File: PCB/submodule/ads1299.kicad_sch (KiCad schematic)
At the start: 18 parts, among them J20 Conn_01x03, J21 CONN_SUBMODULES, U1 ADS1299IPAG, U2 OPA2376

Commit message: Power supply & TPDs
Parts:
- removed C1: 1uF, symbol Device:C
- removed C2: C, symbol Device:C
- removed J20: Conn_01x03, symbol Connector_Generic:Conn_01x05
- removed unit 3 of U2
- added C14, C16, C17, C18, C19, C20, C21, C22: 4.7uF, symbol Device:C
- added C29: 0.1uF, symbol Device:C
- added C30: 10uF, symbol Device:C
- added C31, C33: 1uF, symbol Device:C
- added C32: 100uF, symbol Device:C
- added J1, J18, J19, J2, J3, J4, J5, J8: Conn_01x01_Pin, symbol Connector:Conn_01x01_Pin
- added JP10, JP11, JP12, JP13, JP14, JP15, JP8, JP9: SolderJumper_2_Bridged, symbol Jumper:SolderJumper_2_Bridged
- added R14, R16, R17: 10k, symbol Device:R
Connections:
- net AGND: now also U1.25 (VREFN), C14.1, C16.1, C17.1, C18.1, C19.1, C20.1, C21.1, C22.1, C29.2, C30.2, C31.2, C32.2, C33.2, JP10.1 (A), JP11.1 (A), JP12.1 (A), JP13.1 (A), JP14.1 (A), JP15.1 (A), JP8.1 (A), JP9.1 (A)
- net DGND: now also U1.31 (RESV1), U1.49 (DGND), U1.51 (DGND), R17.1
- net IN1-: now also C22.2, J19.1 (Pin_1), JP15.2 (B)
- net IN2-: now also C21.2, J18.1 (Pin_1), JP14.2 (B)
- net IN3-: now also C20.2, J8.1 (Pin_1), JP13.2 (B)
- net IN4-: now also C19.2, J5.1 (Pin_1), JP12.2 (B)
- net IN5-: now also C18.2, J4.1 (Pin_1), JP11.2 (B)
- net IN6-: now also C17.2, J3.1 (Pin_1), JP10.2 (B)
- net IN7-: now also C16.2, J2.1 (Pin_1), JP9.2 (B)
- net IN8-: now also C14.2, J1.1 (Pin_1), JP8.2 (B)
- net AVDD: now reaches U1.19 (AVDD)
- net AVDD: now also U1.21 (AVDD), U1.22 (AVDD)
- net AVSS: now reaches U1.20 (AVSS)
- net AVSS: now also U1.23 (AVSS), U1.32 (AVSS)
- net at U1.24 (VREFP): now also C29.1, C30.1
- net at U1.26 (VCAP4): now also C31.1
- net at U1.28 (VCAP1): now also C33.1
- net at U1.30 (VCAP2): now also C32.1
- net PWDN: now reaches U1.35 (*PWDN)
- net PWDN: now also R14.1
- net RESET: now reaches U1.36 (*RESET)
- net RESET: now also R16.1
- net START: now reaches U1.38 (START)
- net START: now also R17.2
- net GPIO1: now reaches U1.42 (GPIO1)
- net GPIO2: now reaches U1.44 (GPIO2)
- net GPIO3: now reaches U1.45 (GPIO3)
- net GPIO4: now reaches U1.46 (GPIO4)
- net DVDD: now reaches U1.48 (DVDD)
- net DVDD: now also U1.50 (DVDD), R14.2, R16.2
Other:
- note added: "CONECTOR AL OTRO SUBMODULO OJOOO! AGREGAR ALIMENTACION"
- note added: "Optional Differential Inputs"
- note added: "SB_DAISY_MODE SB_DATAOUT: - BASE = 2-3 | 2-3 - AUX = 2-1 | 2-1 #Ref. ADS1299 datasheet: Section 10.1.4.2 TODO: Tabla"
- note removed: "AGREGAR CAP Y SB PARA CANALES N"
- note removed: "Agregar DGND al micro"
- note removed: "CONECTOR A MICRO"
- note removed: "CONECTOR AL OTRO SUBMODULO"
- note removed: "Consideramos las alimentaciones resuetlas en la placa main"
- note removed: "OJO! Agregar gitignore para KICAD"
- note removed: "SB_DAISY_MODE SB_DATAOUT: - BASE = 2-3 | 2-3 - AUX = 2-1 | 2-1 #Ref. datasheet: Section 10.1.4.2 TODO: Tabla"
- moved on the sheet: C3

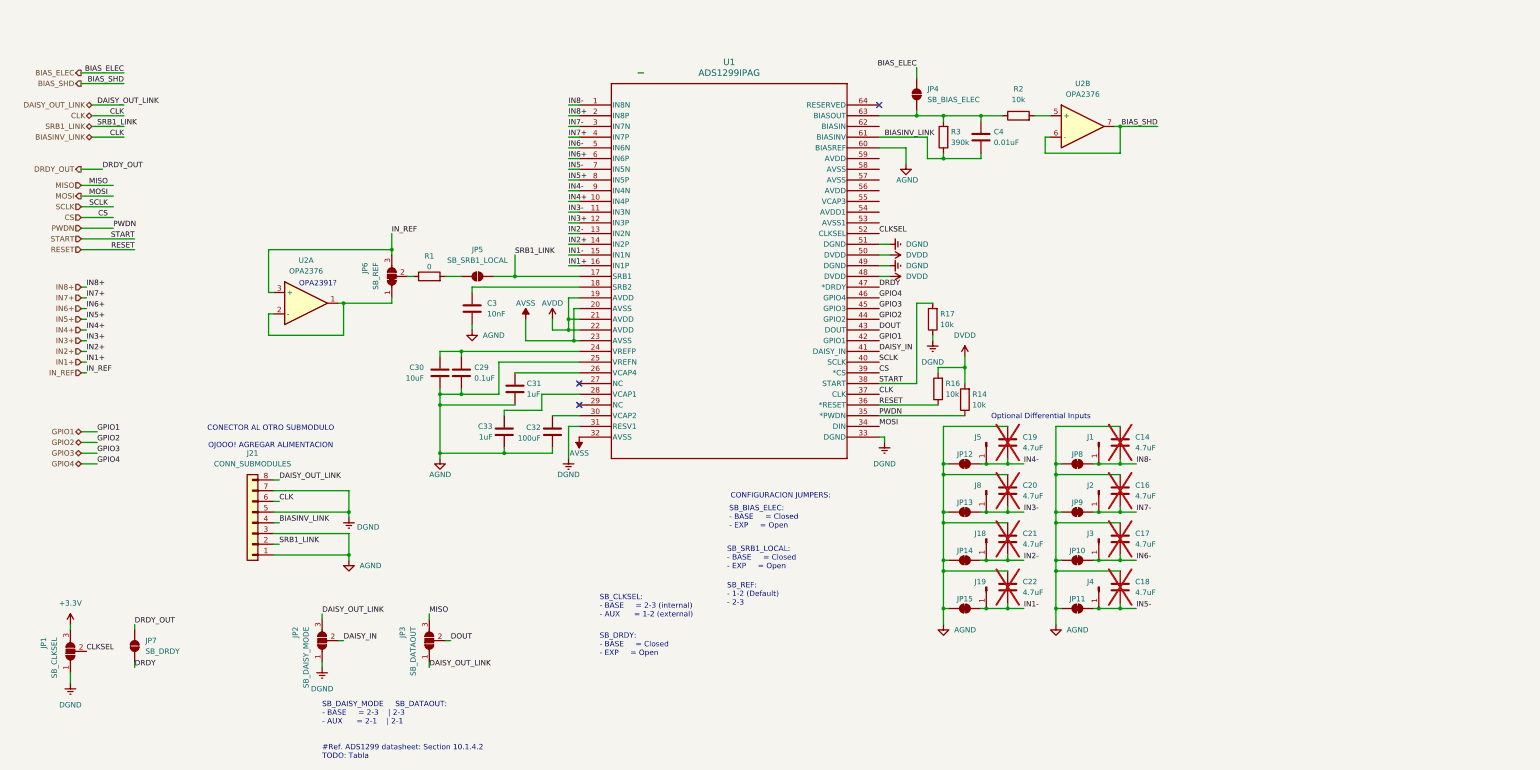
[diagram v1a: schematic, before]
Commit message: draft initial wiring for submodule (pending pin check)
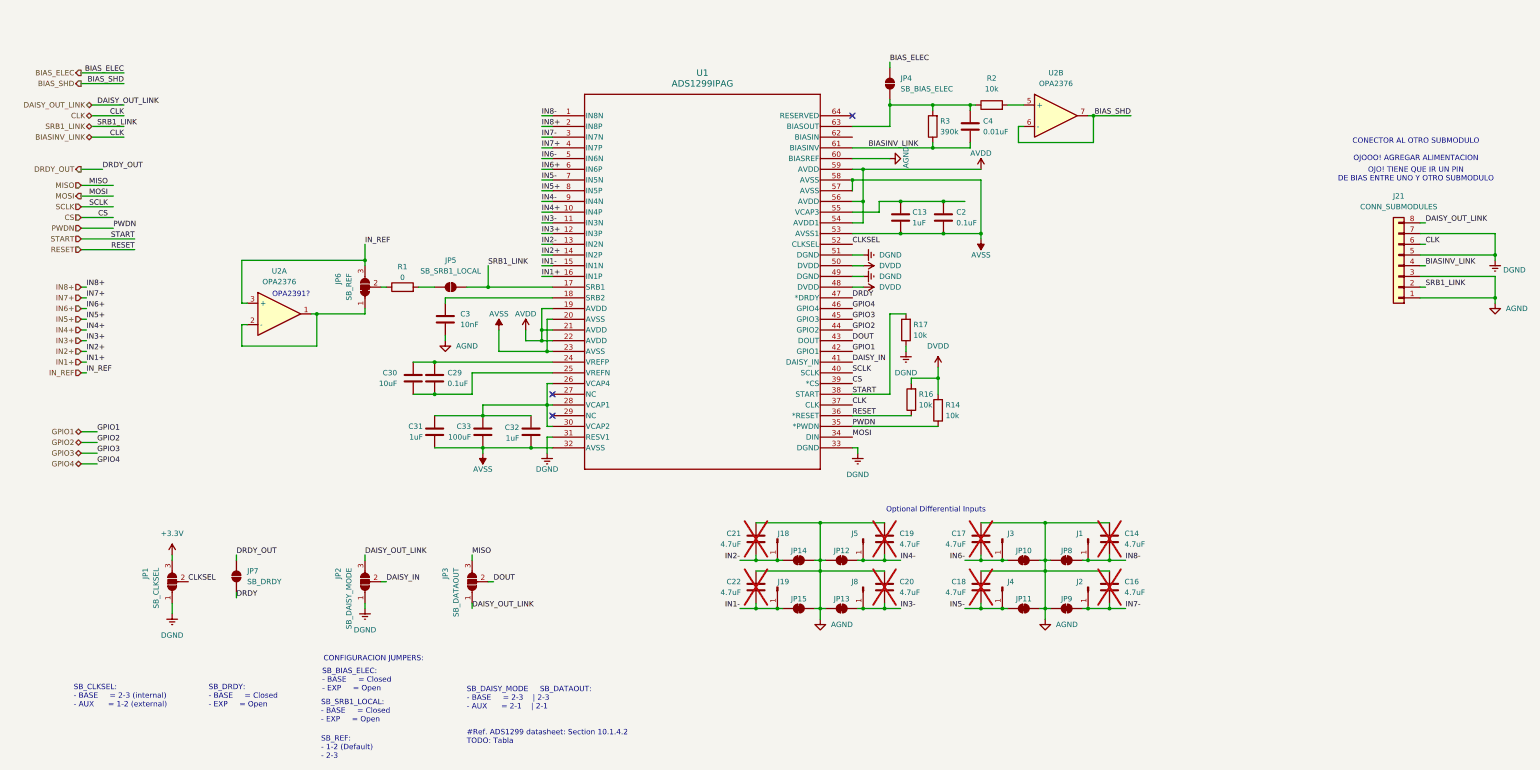
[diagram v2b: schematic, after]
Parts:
- added C13: 1uF, symbol Device:C
- added C2: 0.1uF, symbol Device:C
- C32: value 100uF -> 1uF
- C33: value 1uF -> 100uF
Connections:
- net AGND: no longer C29.2, C30.2, C31.2, C32.2, C33.2, U1.25 (VREFN)
- net AVDD: now also U1.54 (AVDD1), U1.56 (AVDD), U1.59 (AVDD)
- net AVSS: now also C31.2, C32.2, C33.2, U1.53 (AVSS1), U1.57 (AVSS), U1.58 (AVSS), C13.2, C2.2
- net at C33.1, U1.28 (VCAP1): now also C31.1, C32.1, U1.26 (VCAP4), U1.30 (VCAP2)
- net at U1.55 (VCAP3): now also C13.1, C2.1
- new net: C29.2, C30.2, U1.25 (VREFN)
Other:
- note added: "OJO! TIENE QUE IR UN PIN DE BIAS ENTRE UNO Y OTRO SUBMODULO"
- moved on the sheet: C14, C16, C17, C18, C19, C20, C21, C22, C29, C3, C30, C31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

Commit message: fix BIAS (pending ERC & footprints)
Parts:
- removed J21: CONN_SUBMODULES, symbol Connector_Generic:Conn_01x08
- added C15, C35, C37, C39, C41, C43, C44: 1uF, symbol Device:C
- added C36, C38, C40, C42: 0.1uF, symbol Device:C
- added J10, J11: Conn_01x01_Pin, symbol Connector:Conn_01x01_Pin
- added JP17: SB_BIASREF, symbol Jumper:SolderJumper_2_Open
- added U5: OPA2376xxD, symbol Amplifier_Operational:OPA2376xxD
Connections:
- net AGND: now also C37.2, C38.2, C39.2, C40.2, C41.2, C42.2; no longer U1.60 (BIASREF)
- net AVDD: now also C37.1, C38.1, C39.1, C40.1, C41.1, C42.1, C44.1; no longer U1.54 (AVDD1)
- net AVSS: now also C15.2, C43.1
- net DGND: now also C35.2, C36.2
- net DVDD: now also C35.1, C36.1
- net at U1.62 (BIASIN): now also J10.1 (Pin_1)
- new net: C44.2, U5.8 (V+)
- new net: JP17.1 (A), U1.60 (BIASREF)
- new net: J11.1 (Pin_1), JP17.2 (B)
- new net: C15.1, U1.54 (AVDD1)
- new net: C43.2, U5.4 (V-)
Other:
- note added: "SB_BIASREF: - BASE = Open (default) - EXP = Open (default)"
- note removed: "CONECTOR AL OTRO SUBMODULO OJOOO! AGREGAR ALIMENTACION"
- note removed: "OJO! TIENE QUE IR UN PIN DE BIAS ENTRE UNO Y OTRO SUBMODULO"
- moved on the sheet: C13, C2, C4, JP4, R2, R3, U2B
